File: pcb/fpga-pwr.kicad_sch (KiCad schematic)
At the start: 6 parts, among them M1V0 TestPoint, M1V2 TestPoint, U5 XC7A35T-FGG484

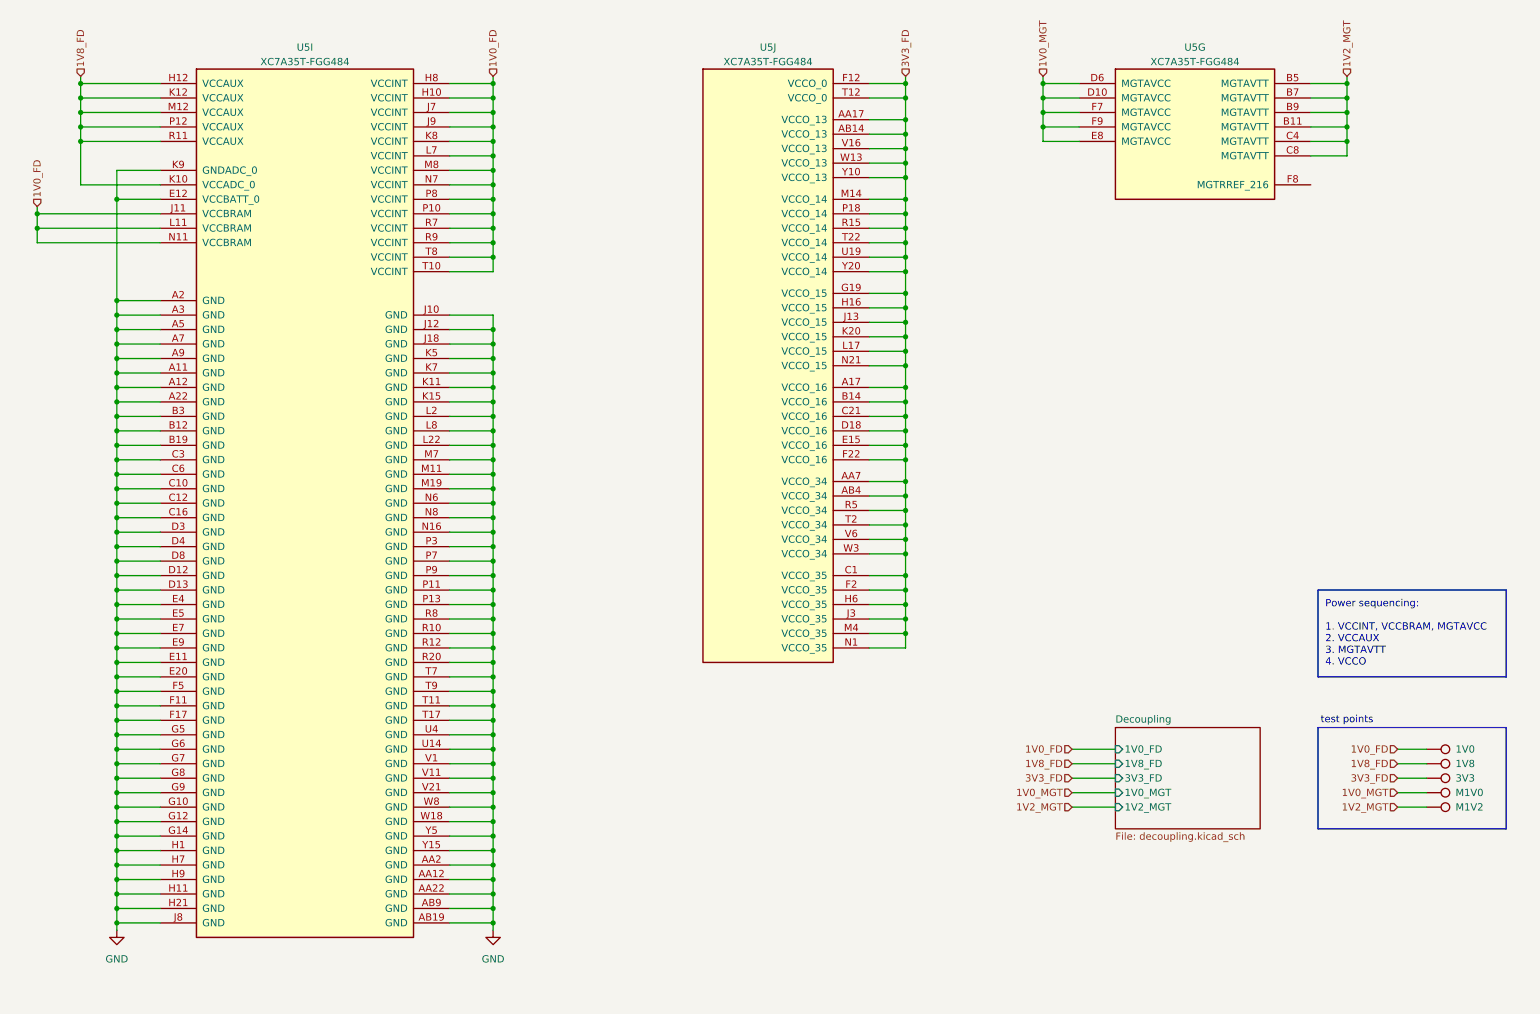
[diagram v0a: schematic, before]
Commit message: defined memory pinouts
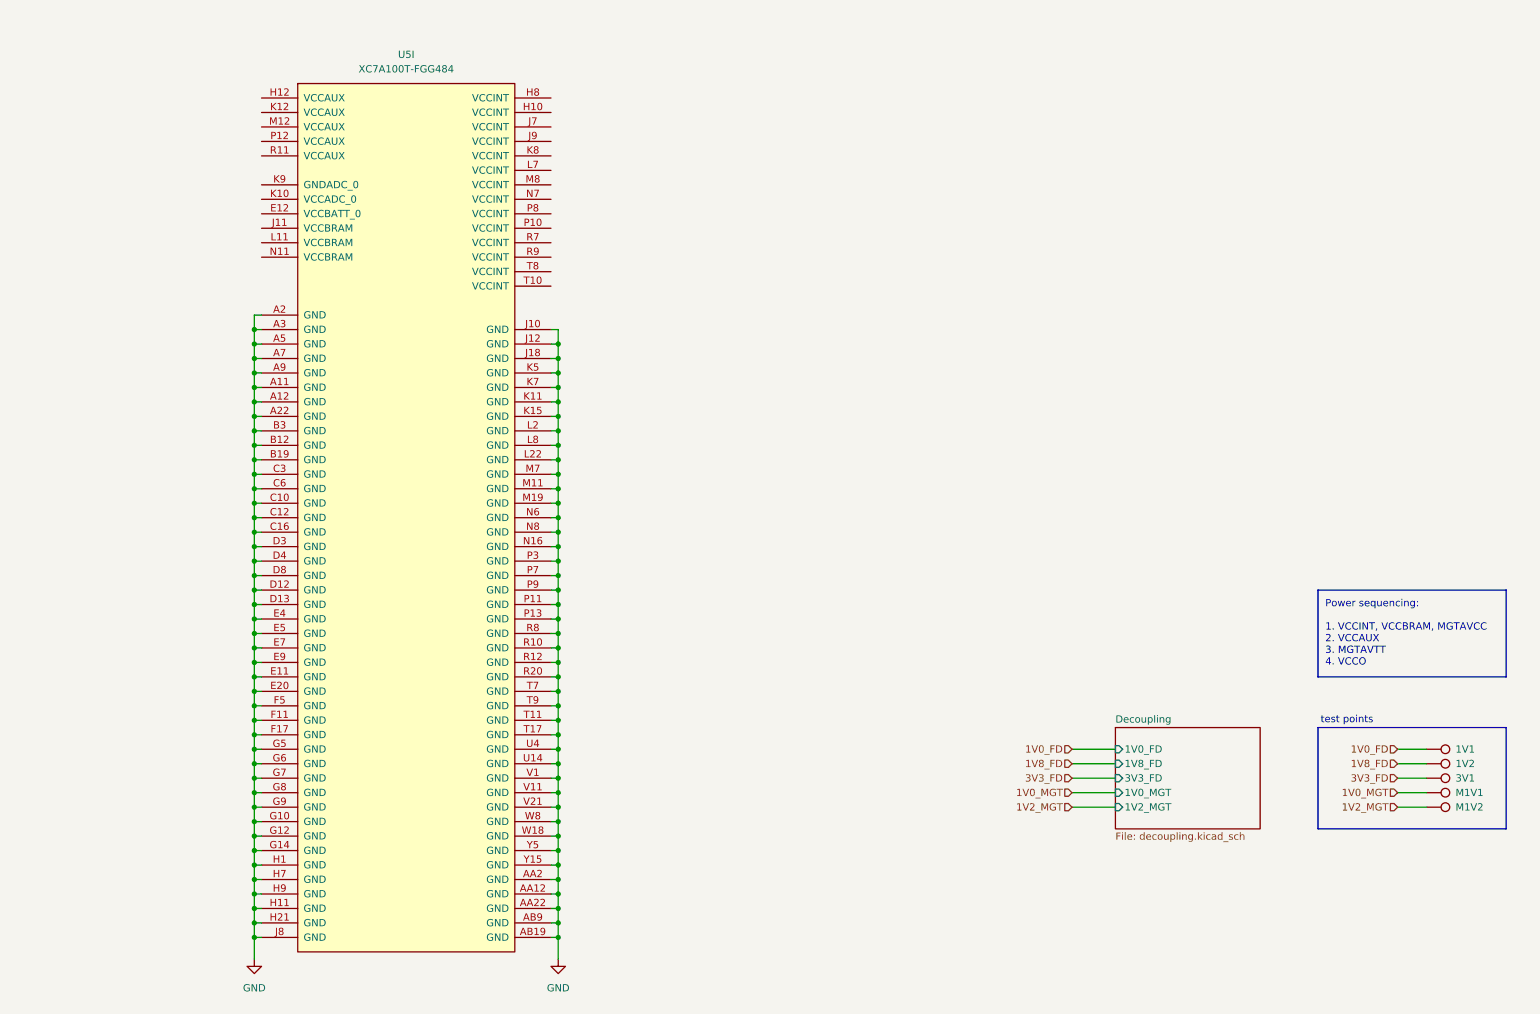
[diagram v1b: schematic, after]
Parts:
- removed U5: XC7A35T-FGG484, Package_BGA:Xilinx_FGG484, symbol library:XC7A35T-FGG484
- added U5: XC7A100T-FGG484, library:Xilinx_FGG484, symbol FPGA_Xilinx_Artix7:XC7A100T-FGG484
- renumbered 1V0 to 1V1, 1V8 to 1V2, 3V3 to 3V1, M1V0 to M1V1
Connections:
- net GND: now also U5.A11 (GND), U5.A12 (GND), U5.A2 (GND), U5.A22 (GND), U5.A3 (GND), U5.A5 (GND), U5.A7 (GND), U5.A9 (GND), U5.AA12 (GND), U5.AA2 (GND), U5.AA22 (GND), U5.AB19 (GND), U5.AB9 (GND), U5.B12 (GND), U5.B19 (GND), U5.B3 (GND), U5.C10 (GND), U5.C12 (GND), U5.C16 (GND), U5.C3 (GND), U5.C6 (GND), U5.D12 (GND), U5.D13 (GND), U5.D3 (GND), U5.D4 (GND), U5.D8 (GND), U5.E11 (GND), U5.E20 (GND), U5.E4 (GND), U5.E5 (GND), U5.E7 (GND), U5.E9 (GND), U5.F11 (GND), U5.F17 (GND), U5.F5 (GND), U5.G10 (GND), U5.G12 (GND), U5.G14 (GND), U5.G5 (GND), U5.G6 (GND), U5.G7 (GND), U5.G8 (GND), U5.G9 (GND), U5.H1 (GND), U5.H11 (GND), U5.H21 (GND), U5.H7 (GND), U5.H9 (GND), U5.J10 (GND), U5.J12 (GND), U5.J18 (GND), U5.J8 (GND), U5.K11 (GND), U5.K15 (GND), U5.K5 (GND), U5.K7 (GND), U5.L2 (GND), U5.L22 (GND), U5.L8 (GND), U5.M11 (GND), U5.M19 (GND), U5.M7 (GND), U5.N16 (GND), U5.N6 (GND), U5.N8 (GND), U5.P11 (GND), U5.P13 (GND), U5.P3 (GND), U5.P7 (GND), U5.P9 (GND), U5.R10 (GND), U5.R12 (GND), U5.R20 (GND), U5.R8 (GND), U5.T11 (GND), U5.T17 (GND), U5.T7 (GND), U5.T9 (GND), U5.U14 (GND), U5.U4 (GND), U5.V1 (GND), U5.V11 (GND), U5.V21 (GND), U5.W18 (GND), U5.W8 (GND), U5.Y15 (GND), U5.Y5 (GND)

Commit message: power restructuring
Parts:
- U5: symbol FPGA_Xilinx_Artix7:XC7A100T-FGG484 -> library:XC7A100T-FGG484
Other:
- moved on the sheet: 1V1, 1V2, 3V1, M1V1, M1V2, U5I

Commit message: changes to power tree
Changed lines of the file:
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@@
+		)
+	)
+	(hierarchical_label "1V35_DDR"
+		(shape input)
+		(at 195.58 137.16 0)
+		(effects
+			(font
+				(size 1.27 1.27)
+			)
+			(justify left)
 		)
 	)

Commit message: moved stuff around, bom
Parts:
- renumbered 1V1 to 1V5, 1V2 to 1V6, U5 to U7
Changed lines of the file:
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@@
 		(on_board yes)
 		(dnp no)
-		(property "Reference" "1V1"
+		(property "Reference" "1V5"
 			(at 269.24 144.78 90)
 			(effects
@@
 			(project "RPi-HwAB-1"
 				(path "/e63e39d7-6ac0-4ffd-8aa3-1841a4541b55/59d21473-a004-4514-8090-fd93db818925/94db1840-7840-4b32-9939-76c2575d480c"
-					(reference "1V1")
+					(reference "1V5")
 					(unit 1)
 				)
@@
 		(dnp no)
 		(fields_autoplaced yes)
-		(property "Reference" "#PWR024"
+		(property "Reference" "#PWR027"
 			(at 111.76 189.23 0)
 			(effects
@@
 			(project "RPi-HwAB-1"
 				(path "/e63e39d7-6ac0-4ffd-8aa3-1841a4541b55/59d21473-a004-4514-8090-fd93db818925/94db1840-7840-4b32-9939-76c2575d480c"
-					(reference "#PWR024")
+					(reference "#PWR027")
 					(unit 1)
 				)
@@
 		(dnp no)
 		(fields_autoplaced yes)
-		(property "Reference" "U5"
+		(property "Reference" "U7"
 			(at 83.82 25.4 0)
 			(effects
@@
 			(project "RPi-HwAB-1"
 				(path "/e63e39d7-6ac0-4ffd-8aa3-1841a4541b55/59d21473-a004-4514-8090-fd93db818925/94db1840-7840-4b32-9939-76c2575d480c"
-					(reference "U5")
+					(reference "U7")
 					(unit 9)
 				)
@@
 		(on_board yes)
 		(dnp no)
-		(property "Reference" "1V2"
+		(property "Reference" "1V6"
 			(at 269.24 147.32 90)
 			(effects
@@
 			(project "RPi-HwAB-1"
 				(path "/e63e39d7-6ac0-4ffd-8aa3-1841a4541b55/59d21473-a004-4514-8090-fd93db818925/94db1840-7840-4b32-9939-76c2575d480c"
-					(reference "1V2")
+					(reference "1V6")
 					(unit 1)
 				)
@@
 		(dnp no)
 		(fields_autoplaced yes)
-		(property "Reference" "#PWR037"
+		(property "Reference" "#PWR026"
 			(at 55.88 189.23 0)
 			(effects
@@
 			(project "RPi-HwAB-1"
 				(path "/e63e39d7-6ac0-4ffd-8aa3-1841a4541b55/59d21473-a004-4514-8090-fd93db818925/94db1840-7840-4b32-9939-76c2575d480c"
-					(reference "#PWR037")
+					(reference "#PWR026")
 					(unit 1)
 				)
@@
 			(project "RPi-HwAB-1"
 				(path "/e63e39d7-6ac0-4ffd-8aa3-1841a4541b55/59d21473-a004-4514-8090-fd93db818925/94db1840-7840-4b32-9939-76c2575d480c"
-					(page "5")
-				)
-			)
+					(page "15")
+				)
+			)

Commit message: jtag, dcplng
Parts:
- added C25: 47uF, Capacitor_SMD:C_0603_1608Metric, symbol library:C
- added C30: 10uF, Capacitor_SMD:C_0402_1005Metric, symbol library:C
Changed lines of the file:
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@@
+	)
+	(symbol
+		(lib_id "library:C")
+		(at 187.96 88.9 0)
+		(unit 1)
+		(exclude_from_sim no)
+		(in_bom yes)
+		(on_board yes)
+		(dnp no)
+		(property "Reference" "C25"
+			(at 189.23 86.36 0)
+			(effects
+				(font
+					(size 1.27 1.27)
+				)
+				(justify left)
+			)
+		)
+		(property "Value" "47uF"
+			(at 189.23 91.44 0)
+			(effects
+				(font
+					(size 1.27 1.27)
+				)
+				(justify left)
+			)
+		)
+		(property "Footprint" "Capacitor_SMD:C_0603_1608Metric"
+			(at 188.9252 92.71 0)
+			(effects
+				(font
+					(size 1.27 1.27)
+				)
+				(hide yes)
+			)
+		)
+		(property "Datasheet" "~"
+			(at 187.96 88.9 0)
+			(effects
+				(font
+					(size 1.27 1.27)
+				)
+				(hide yes)
+			)
+		)
+		(property "Description" "Unpolarized capacitor"
+			(at 187.96 88.9 0)
+			(effects
+				(font
+					(size 1.27 1.27)
+				)
+				(hide yes)
+			)
+		)
+		(property "Name" ""
+			(at 187.96 88.9 0)
+			(effects
+				(font
+					(size 1.27 1.27)
+				)
+				(hide yes)
+			)
+		)
+		(pin "1"
+		)
+		(pin "2"
+		)
+		(instances
+			(project "RPi-HwAB-1"
+				(path "/e63e39d7-6ac0-4ffd-8aa3-1841a4541b55/59d21473-a004-4514-8090-fd93db818925/94db1840-7840-4b32-9939-76c2575d480c"
+					(reference "C25")
+					(unit 1)
+				)
+			)
+		)
+	)
+	(symbol
+		(lib_id "library:C")
+		(at 196.85 88.9 0)
+		(unit 1)
+		(exclude_from_sim no)
+		(in_bom yes)
+		(on_board yes)
+		(dnp no)
+		(property "Reference" "C30"
+			(at 198.12 86.36 0)
+			(effects
+				(font
+					(size 1.27 1.27)
+				)
+				(justify left)
+			)
+		)
+		(property "Value" "10uF"
+			(at 198.12 91.44 0)
+			(effects
+				(font
+					(size 1.27 1.27)
+				)
+				(justify left)
+			)
+		)
+		(property "Footprint" "Capacitor_SMD:C_0402_1005Metric"
+			(at 197.8152 92.71 0)
+			(effects
+				(font
+					(size 1.27 1.27)
+				)
+				(hide yes)
+			)
+		)
+		(property "Datasheet" "~"
+			(at 196.85 88.9 0)
+			(effects
+				(font
+					(size 1.27 1.27)
+				)
+				(hide yes)
+			)
+		)
+		(property "Description" "Unpolarized capacitor"
+			(at 196.85 88.9 0)
+			(effects
+				(font
+					(size 1.27 1.27)
+				)
+				(hide yes)
+			)
+		)
+		(property "Name" ""
+			(at 196.85 88.9 0)
+			(effects
+				(font
+					(size 1.27 1.27)
+				)
+				(hide yes)
+			)
+		)
+		(pin "1"
+		)
+		(pin "2"
+		)
+		(instances
+			(project "RPi-HwAB-1"
+				(path "/e63e39d7-6ac0-4ffd-8aa3-1841a4541b55/59d21473-a004-4514-8090-fd93db818925/94db1840-7840-4b32-9939-76c2575d480c"
+					(reference "C30")
+					(unit 1)
+				)
+			)
+		)
 	)
 	(symbol

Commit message: decoupling
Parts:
- removed 1V5, 1V6, 3V1, M1V1, M1V2: TestPoint, TestPoint:TestPoint_Pad_D1.0mm, symbol library:TestPoint
- added C109, C173, C179, C187, C21: 47uF, Capacitor_SMD:C_0603_1608Metric, symbol library:C
- added C158, C174, C180, C188, C22: 10uF, Capacitor_SMD:C_0402_1005Metric, symbol library:C
- added C159, C160, C161, C162, C163, C164, C165, C166, C167, C168, C169, C170, C171, C172, C175, C176, C177, C178, C181, C182, C183, C184, C185, C186: 0.1uF, Capacitor_SMD:C_0402_1005Metric, symbol library:C
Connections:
- net 1V0_FD: now also U7.E12 (VCCBATT_0), U7.H10 (VCCINT), U7.H8 (VCCINT), U7.J11 (VCCBRAM), U7.J7 (VCCINT), U7.J9 (VCCINT), U7.K8 (VCCINT), U7.L11 (VCCBRAM), U7.L7 (VCCINT), U7.M8 (VCCINT), U7.N11 (VCCBRAM), U7.N7 (VCCINT), U7.P10 (VCCINT), U7.P8 (VCCINT), U7.R7 (VCCINT), U7.R9 (VCCINT), U7.T10 (VCCINT), U7.T8 (VCCINT), C159.2, C160.2, C161.2, C162.2, C163.2, C164.2, C165.2, C166.2, C167.2, C168.2, C169.2, C170.2, C171.2, C172.2, C173.1, C174.1, C175.2, C176.2, C177.2, C178.2
- net 1V0_MGT: now also C25.1, C30.1
- net 1V2_MGT: now also C109.1, C158.1
- net 1V35_DDR: now also C21.1, C22.1
- net 1V8_FD: now also U7.H12 (VCCAUX), U7.K10 (VCCADC_0), U7.K12 (VCCAUX), U7.M12 (VCCAUX), U7.P12 (VCCAUX), U7.R11 (VCCAUX), C179.1, C180.1, C181.2, C182.2, C183.2, C184.2, C185.2, C186.2
- net 3V3_FD: now also C187.1, C188.1
- net GND: now also C25.2, C30.2, U7.K9 (GNDADC_0), C109.2, C158.2, C159.1, C160.1, C161.1, C162.1, C163.1, C164.1, C165.1, C166.1, C167.1, C168.1, C169.1, C170.1, C171.1, C172.1, C173.2, C174.2, C175.1, C176.1, C177.1, C178.1, C179.2, C180.2, C181.1, C182.1, C183.1, C184.1, C185.1, C186.1, C187.2, C188.2, C21.2, C22.2
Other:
- removed sheet Decoupling
- note removed: "test points"
- moved on the sheet: C25, C30, U7I
